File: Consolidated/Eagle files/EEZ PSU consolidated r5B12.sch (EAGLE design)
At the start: 541 parts, among them IC1 LTC3864EMSE#PBF, IC10 DAC8552IDGKTG4, IC11 ADG465SOT-23, IC12 TS5A9411DCKT, IC13 ADS1120IPWR, IC14 LP339D, IC15 TPD4E002DRLR, IC16 TPD2E001DZDR, IC17 ADUM3160BRWZ, IC18 TLC5925IDBQR, IC19 Si8641EC-B-IS1, IC2 LP2951SO8, IC20 SI8651EC-B-IS1, IC21 SI8651EC-B-IS1, IC22 LD1117ADT33TR, IC23 Si8641EC-B-IS1, IC24 PCA21125T/Q900/1,1, IC25 AT25256B-SSHL-B, IC26 W5500, IC27 BC857BS, IC28 TLC555, IC29 SN74LVC08APWR, IC3 TL783CKTTR, IC30 SN74LV1T34DBVR, IC31 TPS3705-33D, IC32 SN74LVC2G02DCTR, IC33 74LVC1G125GW.125, IC34 TPA6205A1DGN, IC4 LTC3260EMSE#PBF, IC5 TL072D, IC6 TL072D, IC7 LTC2050HVCS8#PBF, IC8 MCP23S17-E/SS, IC9 REF5025AIDG4, J1 BS-244DSM-R, J2 1-726388-2, J3 BS-244DSM-G, J4 BS-244DSM-B, J5 BS-244DSM-R, J6 BS-244DSM-B, J7 693072010801, Q1 IRFR5305, Q10 MMBT5401, Q11 MMBT5551, Q12 MMBT5551, Q13 IRLL2705PBF, Q14 IRFR48ZPBF, Q15 IRLML2246TRPBF, Q16 2N7002, Q17 MMBT5551, Q18 MMBT5401, Q19 MMBT5551, Q2 MMBT5401, Q20 MMBT5551, Q21 BTA26-600, Q22 BTA26-600, Q23 IRLL2705PBF, Q24 2N7002, Q25 2N7002, Q26 IRLML2246TRPBF, Q27 IRLML2246TRPBF, Q28 IRLML2246TRPBF, Q29 IRLML2246TRPBF, Q3 2N7002, Q30 2N7002, Q31 IRLML2246TRPBF, Q32 2N7002, Q33 2N7002, Q4 IRFP250N, Q5 BC857C, Q6 BCP56-16.115, Q7 IRFR5305, Q8 BCP56-16.115, Q9 MMBT5401, SW1 A101SYCQ04, SW2 EC12E20-24P24C-SW, SW3 1301.9316, X1 39-30-1039, X10 826629-5, X11 2411-01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

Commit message: #31
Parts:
- added R176: 1M, rcl:R-EU_R0805
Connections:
- net N$111: now also R176.2
- net N$112: now also R176.1
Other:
- moved on the sheet: C116, C120
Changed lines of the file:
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@@
 <setting verticaltext="up"/>
 </settings>
-<grid distance="0.1" unitdist="inch" unit="inch" style="lines" multiple="1" display="no" altdistance="0.01" altunitdist="inch" altunit="inch"/>
+<grid distance="0.025" unitdist="inch" unit="inch" style="lines" multiple="4" display="no" altdistance="0.01" altunitdist="inch" altunit="inch"/>
 <layers>
 <layer number="1" name="Top" color="4" fill="1" visible="no" active="no"/>
@@
 <attribute name="SUPPLIER" value="DIODES INC."/>
 </part>
+<part name="R176" library="rcl" deviceset="R-EU_" device="R0805" value="1M"/>
 </parts>
 <sheets>
@@
 </instance>
 <instance part="Y2" gate="A" x="20.32" y="71.12" smashed="yes" rot="MR270">
-<attribute name="NAME" x="17.145" y="70.485" size="1.778" layer="95" rot="MR0"/>
+<attribute name="NAME" x="20.32" y="78.74" size="1.778" layer="95" rot="MR180"/>
 <attribute name="VALUE" x="23.495" y="67.31" size="1.778" layer="96" rot="MR90"/>
 </instance>
-<instance part="SUPPLY86" gate="GND" x="5.08" y="68.58" smashed="yes" rot="MR0">
-<attribute name="VALUE" x="7.62" y="64.77" size="1.778" layer="96" rot="MR0"/>
+<instance part="SUPPLY86" gate="GND" x="5.08" y="73.66" smashed="yes" rot="MR0">
+<attribute name="VALUE" x="6.985" y="69.85" size="1.778" layer="96" rot="MR0"/>
 </instance>
 <instance part="GND1" gate="1" x="99.06" y="45.72" smashed="yes" rot="MR0">
@@
 <attribute name="VALUE" x="125.857" y="25.8826" size="1.778" layer="96" rot="MR0"/>
 </instance>
-<instance part="C116" gate="G$1" x="15.24" y="76.2" smashed="yes" rot="MR90">
-<attribute name="NAME" x="13.081" y="78.486" size="1.778" layer="95" rot="MR0"/>
-<attribute name="VALUE" x="13.081" y="76.581" size="1.778" layer="96" rot="MR0"/>
-</instance>
-<instance part="C120" gate="G$1" x="15.24" y="66.04" smashed="yes" rot="MR90">
-<attribute name="NAME" x="13.081" y="66.421" size="1.778" layer="95" rot="MR0"/>
-<attribute name="VALUE" x="13.081" y="63.881" size="1.778" layer="96" rot="MR0"/>
+<instance part="C116" gate="G$1" x="12.7" y="76.2" smashed="yes" rot="MR90">
+<attribute name="NAME" x="10.541" y="78.486" size="1.778" layer="95" rot="MR0"/>
+<attribute name="VALUE" x="10.541" y="76.581" size="1.778" layer="96" rot="MR0"/>
+</instance>
+<instance part="C120" gate="G$1" x="12.7" y="66.04" smashed="yes" rot="MR90">
+<attribute name="NAME" x="10.541" y="66.421" size="1.778" layer="95" rot="MR0"/>
+<attribute name="VALUE" x="10.541" y="63.881" size="1.778" layer="96" rot="MR0"/>
 </instance>
 <instance part="R138" gate="G$1" x="116.84" y="99.06" smashed="yes" rot="R90">
@@
 <attribute name="VALUE" x="167.005" y="171.45" size="1.778" layer="96"/>
 </instance>
+<instance part="R176" gate="G$1" x="15.24" y="71.12" smashed="yes" rot="MR90">
+<attribute name="NAME" x="13.97" y="71.3486" size="1.778" layer="95" rot="MR0"/>
+<attribute name="VALUE" x="10.795" y="70.612" size="1.778" layer="96" rot="MR180"/>
+</instance>
 </instances>
 <busses>
@@
 <segment>
 <pinref part="SUPPLY86" gate="GND" pin="GND"/>
-<wire x1="10.16" y1="71.12" x2="5.08" y2="71.12" width="0.1524" layer="91"/>
+<wire x1="7.62" y1="76.2" x2="5.08" y2="76.2" width="0.1524" layer="91"/>
 <pinref part="C120" gate="G$1" pin="2"/>
-<wire x1="10.16" y1="66.04" x2="10.16" y2="71.12" width="0.1524" layer="91"/>
+<wire x1="7.62" y1="66.04" x2="7.62" y2="76.2" width="0.1524" layer="91"/>
 <pinref part="C116" gate="G$1" pin="2"/>
-<wire x1="10.16" y1="76.2" x2="10.16" y2="71.12" width="0.1524" layer="91"/>
-<junction x="10.16" y="71.12"/>
+<junction x="7.62" y="76.2"/>
 </segment>
 <segment>
@@
 <wire x1="25.4" y1="71.12" x2="25.4" y2="76.2" width="0.1524" layer="91"/>
 <pinref part="C116" gate="G$1" pin="1"/>
-<wire x1="17.78" y1="76.2" x2="20.32" y2="76.2" width="0.1524" layer="91"/>
+<wire x1="15.24" y1="76.2" x2="20.32" y2="76.2" width="0.1524" layer="91"/>
 <junction x="20.32" y="76.2"/>
+<pinref part="R176" gate="G$1" pin="2"/>
+<junction x="15.24" y="76.2"/>
 </segment>
 </net>
@@
 <wire x1="40.64" y1="68.58" x2="25.4" y2="68.58" width="0.1524" layer="91"/>
 <pinref part="C120" gate="G$1" pin="1"/>
-<wire x1="20.32" y1="66.04" x2="17.78" y2="66.04" width="0.1524" layer="91"/>
+<wire x1="20.32" y1="66.04" x2="15.24" y2="66.04" width="0.1524" layer="91"/>
 <junction x="20.32" y="66.04"/>
+<pinref part="R176" gate="G$1" pin="1"/>
+<junction x="15.24" y="66.04"/>
 </segment>
 </net>

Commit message: X1 rotated
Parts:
- added X21: ZL262-5SG, con-samtec:SSW-105-02-S-S
- C89, C94: value EEEFK1H470P -> UWT1H220MCL
- L1: device EEZ_Lib1:RN114 -> EEZ_Lib1:RN112
- R6: value 0R -> 1R
- X1: value 39-30-1039 -> (none)
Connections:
- net AC_EARTH: now also X3-1.1; no longer X3-5.1
- net AC_IN_L: now also X3-5.1; no longer X3-1.1
- net DC+: now also X1-3.1; no longer X1-1.1
- net DC_OUT: now also X21-5.1
- net EARTH: now also X1-1.1; no longer X1-3.1
- net FB: now also X21-4.1
- net OUT+: now also X21-3.1
- net PREG_OUT: now also X21-2.1
- net V-: now also X21-1.1
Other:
- note added: "DC in+ 3"
- note added: "Earth 1"
- note added: "Pre-regulator tracking (optional)"
- note removed: "DC in+ 1"
- note removed: "Earth 3"
- moved on the sheet: X1-1, X1-3, X3-1, X3-2, X3-4, X3-5

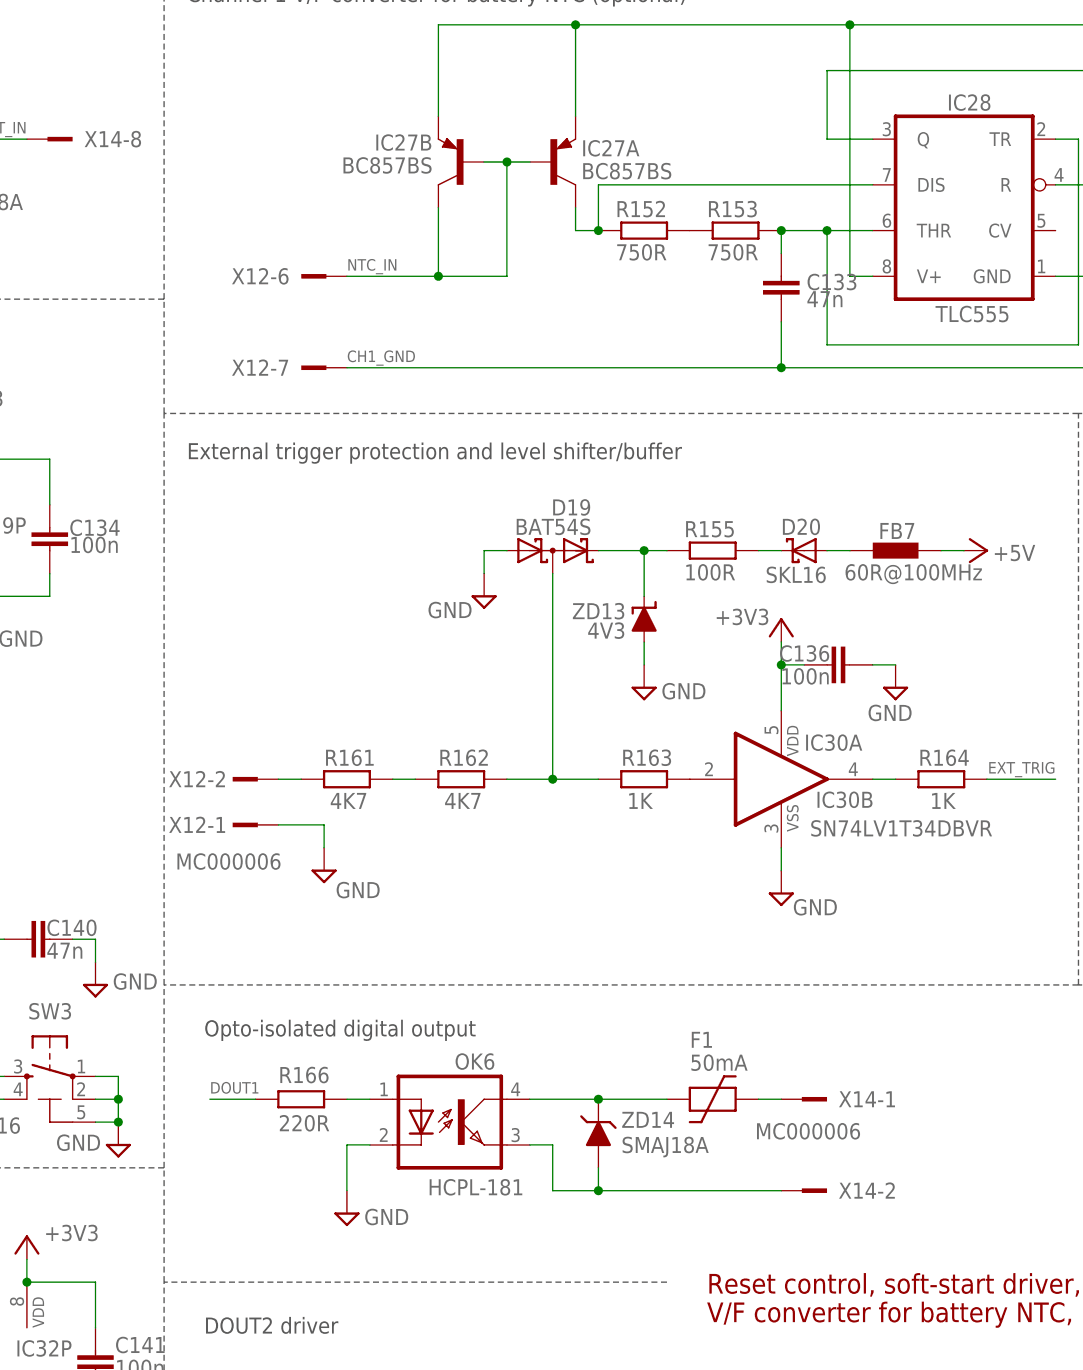
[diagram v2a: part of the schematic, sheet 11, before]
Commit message: X14 pin 1, 2 swap, R177
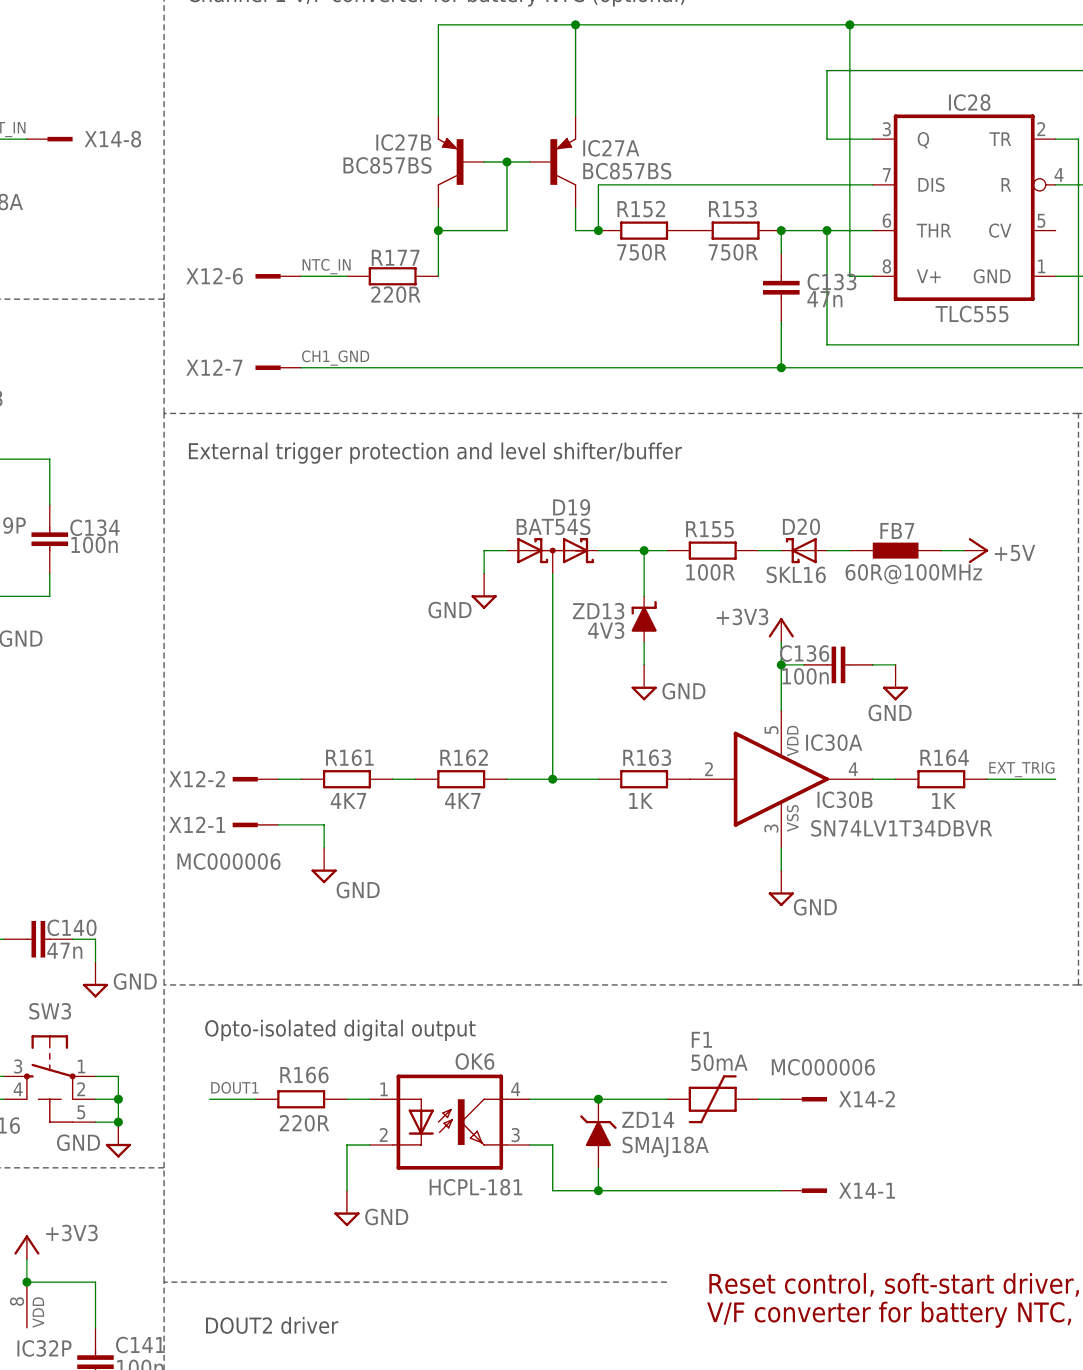
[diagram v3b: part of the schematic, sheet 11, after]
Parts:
- added R177: 220R, rcl:R-EU_R0805
- X1: value (none) -> 39-30-1039
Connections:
- removed net N$189: F1.P$2, X14-1.1
- new net N$46: F1.P$2, X14-2.1
- new net N$59: IC27A.B, IC27B.B, IC27B.C, R177.2
- net N$188: now also X14-1.1; no longer X14-2.1
- net NTC_IN: now also R177.1; no longer IC27A.B, IC27B.B, IC27B.C
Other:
- moved on the sheet: X12-6, X12-7, X14-1, X14-2
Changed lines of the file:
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@@
 <part name="R176" library="rcl" deviceset="R-EU_" device="R0805" value="1M"/>
 <part name="L1" library="EEZ_Lib1" deviceset="RN112" device="" value="RN112-4-02"/>
-<part name="X1" library="EEZ_Lib1" deviceset="MINIFIT_39301039" device=""/>
+<part name="X1" library="EEZ_Lib1" deviceset="MINIFIT_39301039" device="" value="39-30-1039"/>
 <part name="X21" library="con-samtec" deviceset="SSW-105-02-S-S" device="" value="ZL262-5SG">
 <attribute name="MPN" value="SSW-105-02-S-S"/>
 <attribute name="OC_NEWARK" value="11P9399"/>
 </part>
+<part name="R177" library="rcl" deviceset="R-EU_" device="R0805" value="220R"/>
 </parts>
 <sheets>
@@
 <instance part="X1" gate="-1" x="15.24" y="152.4" smashed="yes">
 <attribute name="NAME" x="8.89" y="153.289" size="1.778" layer="95" rot="R180"/>
-<attribute name="VALUE" x="6.35" y="155.067" size="1.778" layer="96"/>
+<attribute name="VALUE" x="3.81" y="174.752" size="1.778" layer="96"/>
 </instance>
 <instance part="X1" gate="-3" x="15.24" y="172.72" smashed="yes">
@@
 <attribute name="VALUE" x="122.555" y="83.058" size="1.778" layer="96"/>
 </instance>
-<instance part="X12" gate="-7" x="124.46" y="132.08"/>
-<instance part="X12" gate="-6" x="124.46" y="142.24"/>
+<instance part="X12" gate="-7" x="119.38" y="132.08"/>
+<instance part="X12" gate="-6" x="119.38" y="142.24"/>
 <instance part="IC29" gate="P" x="83.82" y="114.3" smashed="yes">
 <attribute name="NAME" x="82.55" y="113.665" size="1.778" layer="95"/>
@@
 </instance>
 <instance part="X14" gate="-7" x="63.5" y="144.78"/>
-<instance part="X14" gate="-2" x="172.72" y="40.64" smashed="yes" rot="R180">
-<attribute name="NAME" x="179.07" y="39.751" size="1.778" layer="95"/>
-</instance>
-<instance part="X14" gate="-1" x="172.72" y="50.8" smashed="yes" rot="R180">
+<instance part="X14" gate="-2" x="172.72" y="50.8" smashed="yes" rot="R180">
 <attribute name="NAME" x="179.07" y="49.911" size="1.778" layer="95"/>
-<attribute name="VALUE" x="181.61" y="48.133" size="1.778" layer="96" rot="R180"/>
+</instance>
+<instance part="X14" gate="-1" x="172.72" y="40.64" smashed="yes" rot="R180">
+<attribute name="NAME" x="179.07" y="39.751" size="1.778" layer="95"/>
+<attribute name="VALUE" x="171.45" y="53.467" size="1.778" layer="96"/>
 </instance>
 <instance part="SW2" gate="-1" x="213.36" y="93.98" smashed="yes" rot="MR90">
@@
 <attribute name="VALUE" x="220.599" y="111.506" size="1.778" layer="96"/>
 </instance>
+<instance part="R177" gate="G$1" x="129.54" y="142.24" smashed="yes" rot="MR180">
+<attribute name="NAME" x="127" y="145.1864" size="1.778" layer="95" rot="MR180"/>
+<attribute name="VALUE" x="127" y="141.097" size="1.778" layer="96" rot="MR180"/>
+</instance>
 </instances>
 <busses>
@@
 </segment>
 </net>
-<net name="NTC_IN" class="0">
-<segment>
-<label x="124.46" y="142.875" size="1.27" layer="102"/>
-<pinref part="IC27" gate="B" pin="B"/>
-<pinref part="IC27" gate="A" pin="B"/>
-<wire x1="139.7" y1="154.94" x2="142.24" y2="154.94" width="0.1524" layer="91"/>
-<pinref part="IC27" gate="B" pin="C"/>
-<wire x1="142.24" y1="154.94" x2="144.78" y2="154.94" width="0.1524" layer="91"/>
-<wire x1="142.24" y1="142.24" x2="142.24" y2="154.94" width="0.1524" layer="91"/>
-<junction x="142.24" y="154.94"/>
-<wire x1="134.62" y1="142.24" x2="134.62" y2="149.86" width="0.1524" layer="91"/>
-<wire x1="134.62" y1="142.24" x2="142.24" y2="142.24" width="0.1524" layer="91"/>
-<junction x="134.62" y="142.24"/>
-<wire x1="124.46" y1="142.24" x2="134.62" y2="142.24" width="0.1524" layer="91"/>
-<pinref part="X12" gate="-6" pin="1"/>
-</segment>
-</net>
 <net name="N$136" class="0">
 <segment>
@@
 <junction x="208.28" y="132.08"/>
 <label x="223.52" y="132.715" size="1.27" layer="102" rot="MR0"/>
-<label x="124.46" y="133.985" size="1.27" layer="102" rot="MR180"/>
-<wire x1="172.72" y1="132.08" x2="124.46" y2="132.08" width="0.1524" layer="91"/>
+<label x="119.38" y="132.715" size="1.27" layer="102"/>
+<wire x1="172.72" y1="132.08" x2="119.38" y2="132.08" width="0.1524" layer="91"/>
 <junction x="172.72" y="132.08"/>
 <pinref part="C132" gate="G$1" pin="2"/>
@@
 <wire x1="147.32" y1="40.64" x2="147.32" y2="45.72" width="0.1524" layer="91"/>
 <wire x1="147.32" y1="45.72" x2="144.78" y2="45.72" width="0.1524" layer="91"/>
+<pinref part="OK6" gate="G$1" pin="EMIT"/>
 <wire x1="152.4" y1="40.64" x2="172.72" y2="40.64" width="0.1524" layer="91"/>
 <junction x="152.4" y="40.64"/>
-<pinref part="OK6" gate="G$1" pin="EMIT"/>
-<pinref part="X14" gate="-2" pin="1"/>
+<pinref part="X14" gate="-1" pin="1"/>
 </segment>
 </net>
@@
 </segment>
 </net>
-<net name="N$189" class="0">
-<segment>
-<pinref part="F1" gate="G$1" pin="P$2"/>
-<wire x1="170.18" y1="50.8" x2="172.72" y2="50.8" width="0.1524" layer="91"/>
-<pinref part="X14" gate="-1" pin="1"/>
-</segment>
-</net>
 <net name="N$182" class="0">
 <segment>
@@
 </segment>
 </net>
+<net name="N$46" class="0">
+<segment>
+<pinref part="F1" gate="G$1" pin="P$2"/>
+<wire x1="170.18" y1="50.8" x2="172.72" y2="50.8" width="0.1524" layer="91"/>
+<pinref part="X14" gate="-2" pin="1"/>
+</segment>
+</net>
+<net name="NTC_IN" class="0">
+<segment>
+<pinref part="X12" gate="-6" pin="1"/>
+<label x="119.38" y="142.875" size="1.27" layer="102"/>
+<pinref part="R177" gate="G$1" pin="1"/>
+<wire x1="119.38" y1="142.24" x2="124.46" y2="142.24" width="0.1524" layer="91"/>
+</segment>
+</net>
+<net name="N$59" class="0">
+<segment>
+<pinref part="IC27" gate="B" pin="B"/>
+<pinref part="IC27" gate="A" pin="B"/>
+<wire x1="139.7" y1="154.94" x2="142.24" y2="154.94" width="0.1524" layer="91"/>
+<wire x1="142.24" y1="154.94" x2="144.78" y2="154.94" width="0.1524" layer="91"/>
+<wire x1="142.24" y1="154.94" x2="142.24" y2="147.32" width="0.1524" layer="91"/>
+<junction x="142.24" y="154.94"/>
+<pinref part="IC27" gate="B" pin="C"/>
+<wire x1="142.24" y1="147.32" x2="134.62" y2="147.32" width="0.1524" layer="91"/>
+<wire x1="134.62" y1="147.32" x2="134.62" y2="149.86" width="0.1524" layer="91"/>
+<pinref part="R177" gate="G$1" pin="2"/>
+<wire x1="134.62" y1="142.24" x2="134.62" y2="147.32" width="0.1524" layer="91"/>
+<junction x="134.62" y="147.32"/>
+</segment>
+</net>

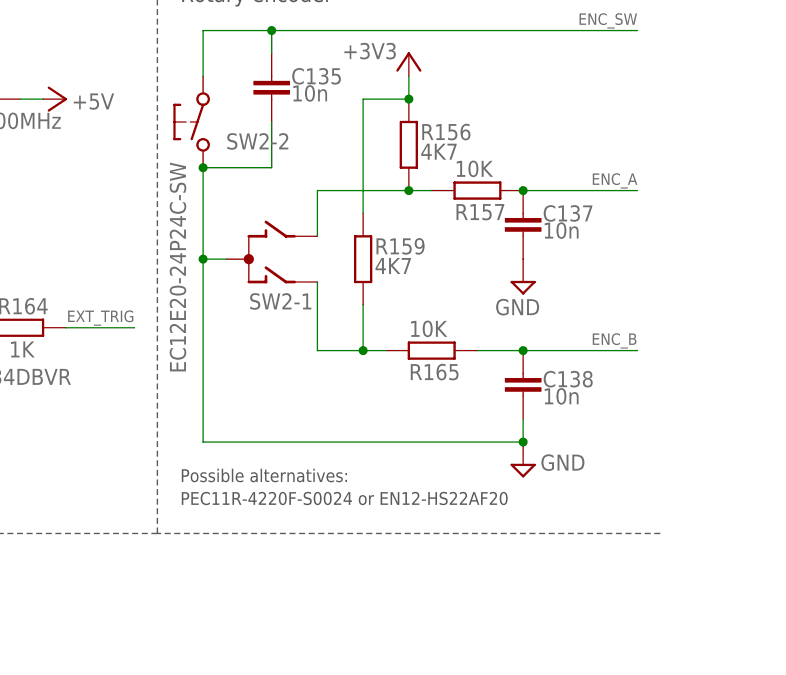
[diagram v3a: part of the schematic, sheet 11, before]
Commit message: Encoder 25mm, new enclosure panels
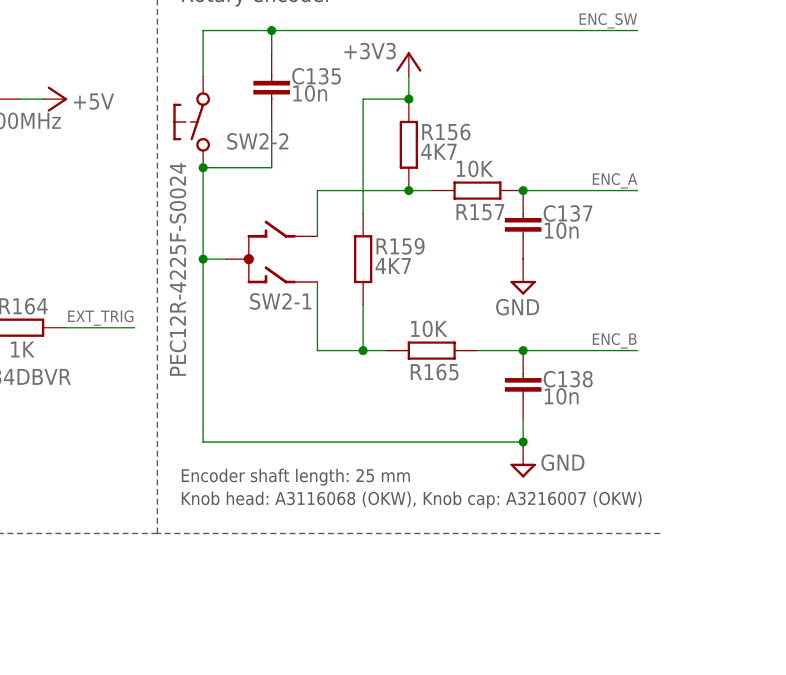
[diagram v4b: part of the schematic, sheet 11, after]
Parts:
- SW2: value EC12E20-24P24C-SW -> PEC12R-4225F-S0024
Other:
- note added: "Encoder shaft length: 25 mm"
- note added: "Knob head: A3116068 (OKW), Knob cap: A3216007 (OKW)"
- note removed: "PEC11R-4220F-S0024 or EN12-HS22AF20"
- note removed: "Possible alternatives:"
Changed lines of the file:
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@@
 <part name="C23" library="EEZ_Lib1" deviceset="ECAP" device="1206" value="10u"/>
 <part name="C31" library="EEZ_Lib1" deviceset="ECAP" device="1206" value="10u"/>
-<part name="SW2" library="EEZ_Lib1" deviceset="ENCODER_SW" device="" value="EC12E20-24P24C-SW"/>
+<part name="SW2" library="EEZ_Lib1" deviceset="ENCODER_SW" device="" value="PEC12R-4225F-S0024"/>
 <part name="D12" library="diode" deviceset="DIODE-" device="SOD323-W" value="BAS316"/>
 <part name="K_DOUT" library="EEZ_Lib1" deviceset="RELAY_RT314012" device="-2" value="RT424005"/>
@@
 <wire x1="261.62" y1="127" x2="205.74" y2="127" width="0.1524" layer="97" style="shortdash"/>
 <wire x1="160.02" y1="30.48" x2="104.14" y2="30.48" width="0.1524" layer="97" style="shortdash"/>
-<text x="208.28" y="69.215" size="1.4224" layer="97">Possible alternatives:</text>
-<text x="208.28" y="66.675" size="1.4224" layer="97">PEC11R-4220F-S0024 or EN12-HS22AF20</text>
+<text x="208.28" y="69.215" size="1.4224" layer="97">Encoder shaft length: 25 mm</text>
+<text x="208.28" y="66.675" size="1.4224" layer="97">Knob head: A3116068 (OKW), Knob cap: A3216007 (OKW)</text>
 </plain>
 <instances>
